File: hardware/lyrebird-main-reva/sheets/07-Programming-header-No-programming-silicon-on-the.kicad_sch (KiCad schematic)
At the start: 4 parts, among them J3 JTAG 2x5 1.27mm

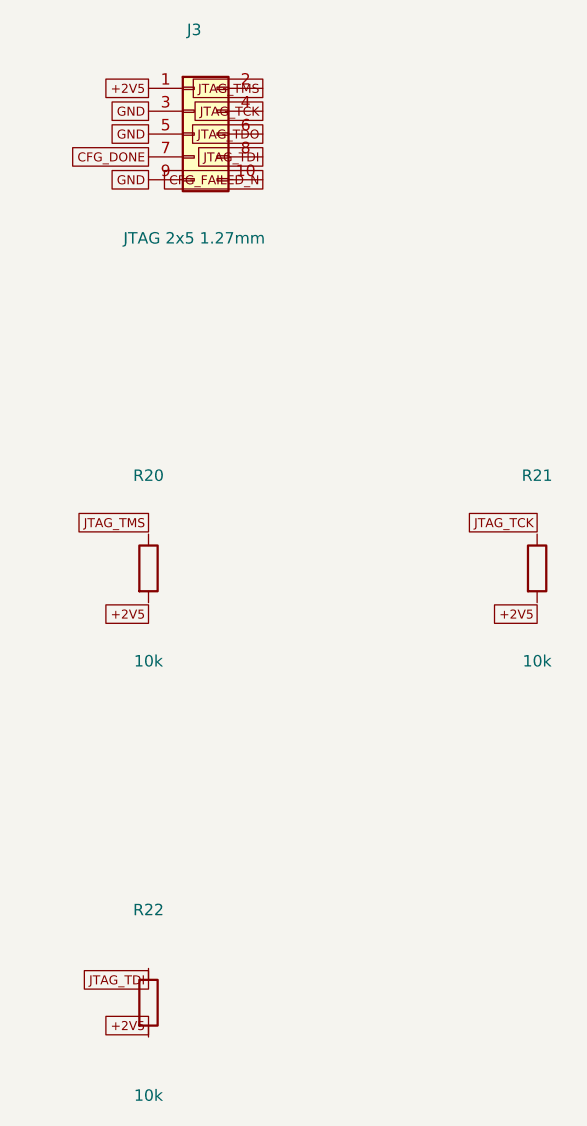
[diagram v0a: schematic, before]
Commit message: Regenerate the schematics, which were eleven days behind the netlists
The sheets and both PDFs dated 13 September against netlists from
today. They showed a board with USB bus power, a charge pump on the
analog module, no JTAG series protection, no oscillator pull-downs and
none of the footprint corrections -- a board that has not existed for
some time. Anyone opening them to review the design would have been
reviewing the wrong one, which is worse than having no schematic.

Regenerated from the current netlists: the main board goes from 8
sheets to 11, picking up the wall-wart input and the inverter, and the
module from 6 to 9 while losing the charge pump entirely. Both PDFs
rebuilt through kicad-cli, one page per sheet.

Nothing regenerated them because nothing was watching. The netlist
generators are run constantly and the views derived from them are not,
so they drift silently and there is no check that notices.

Co-Authored-By: Claude Opus 5 <noreply@anthropic.com>
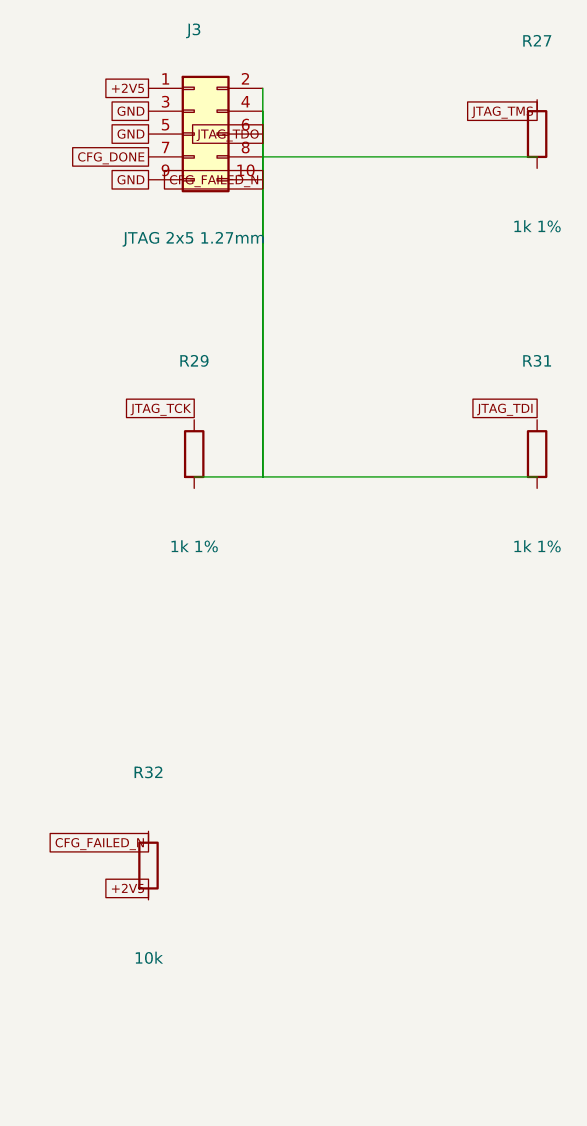
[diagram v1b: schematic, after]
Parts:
- added R32: 10k, symbol Device:R
- R27: renamed from R20; value 10k -> 1k 1%
- R29: renamed from R21; value 10k -> 1k 1%
- R31: renamed from R22; value 10k -> 1k 1%
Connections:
- net JTAG_TDO is gone; now on net CFG_FAILED_N: J3.6 (Pin_6)
- net CFG_FAILED_N: now also J3.2 (Pin_2), J3.4 (Pin_4), J3.8 (Pin_8)
- net JTAG_TCK: no longer J3.4 (Pin_4)
- net JTAG_TDI: no longer J3.8 (Pin_8)
- net JTAG_TMS: no longer J3.2 (Pin_2)
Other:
- moved on the sheet: R27, R29, R31
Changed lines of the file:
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@@
 	(version 20231120)
 	(generator "lyrebird")
-	(paper "User" 128 171)
+	(paper "User" 127 157)
 	(title_block (title "Programming header. No programming silicon on the board: 0006"))
 	(symbol (lib_id "Connector_Generic:Conn_02x05_Odd_Even") (at 40.64 38.1 0) (unit 1)
@@
 		(instances (project "" (path "/" (reference "J3") (unit 1))))
 	)
-	(symbol (lib_id "Device:R") (at 35.56 86.36 0) (unit 1)
+	(symbol (lib_id "Device:R") (at 78.74 38.1 0) (unit 1)
 		(exclude_from_sim no) (in_bom yes) (on_board yes) (dnp no)
-		(property "Reference" "R20" (at 35.56 76.05 0)
+		(property "Reference" "R27" (at 78.74 27.79 0)
 			(effects (font (size 1.27 1.27))))
-		(property "Value" "10k" (at 35.56 96.67 0)
+		(property "Value" "1k 1%" (at 78.74 48.410000000000004 0)
 			(effects (font (size 1.27 1.27))))
-		(instances (project "" (path "/" (reference "R20") (unit 1))))
+		(instances (project "" (path "/" (reference "R27") (unit 1))))
 	)
-	(symbol (lib_id "Device:R") (at 78.74 86.36 0) (unit 1)
+	(symbol (lib_id "Device:R") (at 40.64 73.66 0) (unit 1)
 		(exclude_from_sim no) (in_bom yes) (on_board yes) (dnp no)
-		(property "Reference" "R21" (at 78.74 76.05 0)
+		(property "Reference" "R29" (at 40.64 63.349999999999994 0)
 			(effects (font (size 1.27 1.27))))
-		(property "Value" "10k" (at 78.74 96.67 0)
+		(property "Value" "1k 1%" (at 40.64 83.97 0)
 			(effects (font (size 1.27 1.27))))
-		(instances (project "" (path "/" (reference "R21") (unit 1))))
+		(instances (project "" (path "/" (reference "R29") (unit 1))))
 	)
-	(symbol (lib_id "Device:R") (at 35.56 134.62 0) (unit 1)
+	(symbol (lib_id "Device:R") (at 78.74 73.66 0) (unit 1)
 		(exclude_from_sim no) (in_bom yes) (on_board yes) (dnp no)
-		(property "Reference" "R22" (at 35.56 124.31 0)
+		(property "Reference" "R31" (at 78.74 63.349999999999994 0)
 			(effects (font (size 1.27 1.27))))
-		(property "Value" "10k" (at 35.56 144.93 0)
+		(property "Value" "1k 1%" (at 78.74 83.97 0)
 			(effects (font (size 1.27 1.27))))
-		(instances (project "" (path "/" (reference "R22") (unit 1))))
+		(instances (project "" (path "/" (reference "R31") (unit 1))))
 	)
+	(symbol (lib_id "Device:R") (at 35.56 119.38 0) (unit 1)
+		(exclude_from_sim no) (in_bom yes) (on_board yes) (dnp no)
+		(property "Reference" "R32" (at 35.56 109.07 0)
+			(effects (font (size 1.27 1.27))))
+		(property "Value" "10k" (at 35.56 129.69 0)
+			(effects (font (size 1.27 1.27))))
+		(instances (project "" (path "/" (reference "R32") (unit 1))))
+	)
+	(wire (pts (xy 48.26 35.56) (xy 48.26 76.2))
+		(stroke (width 0) (type default)))
+	(wire (pts (xy 48.26 76.2) (xy 40.64 76.2))
+		(stroke (width 0) (type default)))
+	(wire (pts (xy 48.26 40.64) (xy 48.26 76.2))
+		(stroke (width 0) (type default)))
+	(wire (pts (xy 48.26 76.2) (xy 78.74 76.2))
+		(stroke (width 0) (type default)))
+	(wire (pts (xy 48.26 33.02) (xy 48.26 40.64))
+		(stroke (width 0) (type default)))
+	(wire (pts (xy 48.26 40.64) (xy 78.74 40.64))
+		(stroke (width 0) (type default)))
 	(global_label "+2V5" (shape passive) (at 35.56 33.02 0)
 		(effects (font (size 1.0 1.0)) (justify right))
 )
-	(global_label "+2V5" (shape passive) (at 35.56 91.44 0)
-		(effects (font (size 1.0 1.0)) (justify right))
-)
-	(global_label "+2V5" (shape passive) (at 78.74 91.44 0)
-		(effects (font (size 1.0 1.0)) (justify right))
-)
-	(global_label "+2V5" (shape passive) (at 35.56 137.16 0)
+	(global_label "+2V5" (shape passive) (at 35.56 121.92 0)
 		(effects (font (size 1.0 1.0)) (justify right))
 )
@@
 )
 	(global_label "CFG_FAILED_N" (shape passive) (at 48.26 43.18 0)
+		(effects (font (size 1.0 1.0)) (justify right))
+)
+	(global_label "CFG_FAILED_N" (shape passive) (at 35.56 116.84 0)
 		(effects (font (size 1.0 1.0)) (justify right))
 )
@@
 		(effects (font (size 1.0 1.0)) (justify right))
 )
-	(global_label "JTAG_TCK" (shape passive) (at 48.26 35.56 0)
+	(global_label "JTAG_TCK" (shape passive) (at 40.64 68.58 0)
 		(effects (font (size 1.0 1.0)) (justify right))
 )
-	(global_label "JTAG_TCK" (shape passive) (at 78.74 81.28 0)
-		(effects (font (size 1.0 1.0)) (justify right))
-)
-	(global_label "JTAG_TDI" (shape passive) (at 48.26 40.64 0)
-		(effects (font (size 1.0 1.0)) (justify right))
-)
-	(global_label "JTAG_TDI" (shape passive) (at 35.56 132.08 0)
+	(global_label "JTAG_TDI" (shape passive) (at 78.74 68.58 0)
 		(effects (font (size 1.0 1.0)) (justify right))
 )
@@
 		(effects (font (size 1.0 1.0)) (justify right))
 )
-	(global_label "JTAG_TMS" (shape passive) (at 48.26 33.02 0)
+	(global_label "JTAG_TMS" (shape passive) (at 78.74 35.56 0)
 		(effects (font (size 1.0 1.0)) (justify right))
 )
-	(global_label "JTAG_TMS" (shape passive) (at 35.56 81.28 0)
-		(effects (font (size 1.0 1.0)) (justify right))
-)
